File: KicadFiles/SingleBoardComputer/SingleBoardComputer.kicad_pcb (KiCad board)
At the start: 2 copper layers, 84 parts, among them J1 USB_C_Receptacle_USB2.0_16P, J2 Conn_01x06_Pin, J3 Conn_01x10_Pin, SW1 SW_DPST_x2, U1 TPS630701RNMT, U2 FT240XS, U3 LD1117S33TR_SOT223, U4 MC68000FN, U5 XC9572XL-PC44, U6 SST39SF040-70-4C-PHE, U7 SST39SF040-70-4C-PHE, U8 AS7C1026B-12JCN, Y1 CXO_DIP8

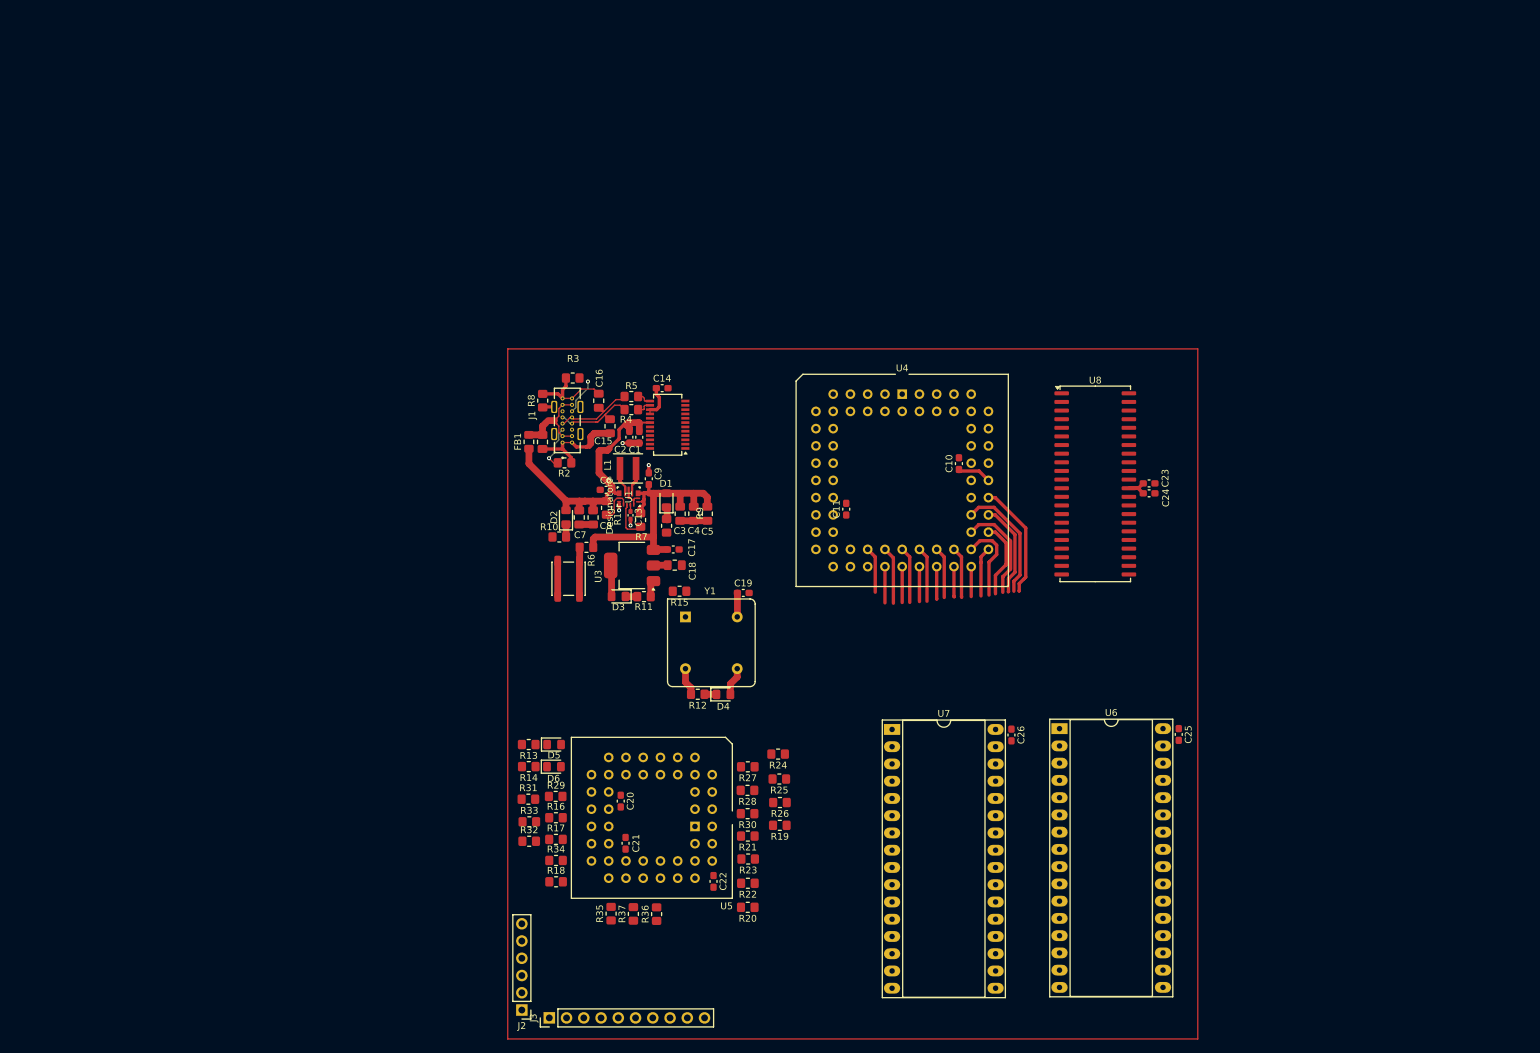
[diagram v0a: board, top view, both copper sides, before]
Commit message: PCB before schematic modification
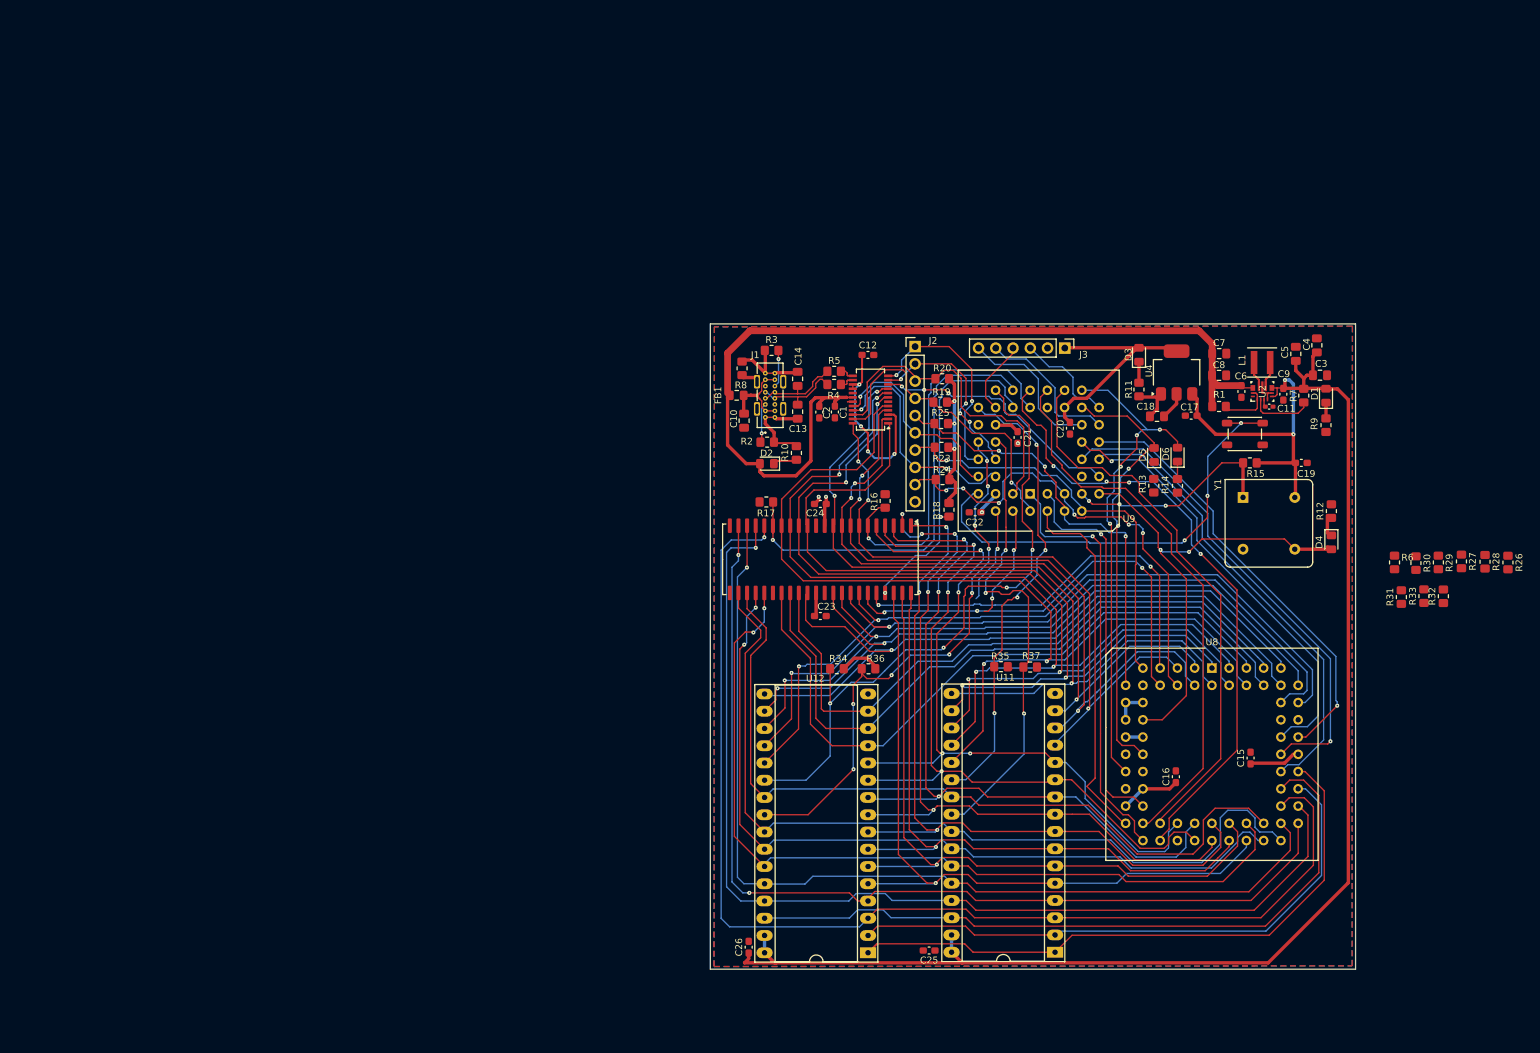
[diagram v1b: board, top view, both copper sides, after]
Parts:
- removed R21, R22: 5.1k, Resistor_SMD:R_0805_2012Metric_Pad1.20x1.40mm_HandSolder
- L1: value L -> 1.5u
- moved R32 139.3 mm to (210.8, 83.4), turned to 90 degrees
- moved R33 135.8 mm to (207.9, 83.4), turned to 90 degrees
- moved R29 134.4 mm to (210.1, 78.5), turned to -90 degrees
- moved R31 131.9 mm to (204.6, 83.5), turned to 90 degrees
- moved J3 126.1 mm to (155.1, 46.9), turned to -90 degrees
- moved R6 119.0 mm to (203.6, 78.5), turned to -90 degrees
- moved R28 113.7 mm to (216.9, 78.3), turned to -90 degrees
- moved R26 112.9 mm to (220.3, 78.5), turned to -90 degrees
- moved J2 112.6 mm to (133.0, 46.7), turned to 0 degrees
- moved R27 109.3 mm to (213.4, 78.3), turned to -90 degrees
- moved R30 105.1 mm to (206.8, 78.5), turned to -90 degrees
- moved R14 104.1 mm to (171.6, 67.2), turned to -90 degrees
- moved D6 102.7 mm to (171.7, 62.6), turned to 90 degrees
- moved SW1 101.8 mm to (181.6, 59.5), turned to 0 degrees
- moved R13 99.6 mm to (168.2, 67.2), turned to -90 degrees
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- renumbered C12 to C10, C13 to C11, C14 to C12, C15 to C13, C16 to C14, C10 to C15, C11 to C16, J3 to J2, J2 to J3, U8 to U10, U6 to U11, U7 to U12, U1 to U2, U2 to U3, U3 to U4, U4 to U8, U5 to U9
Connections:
- U9 pad 40: RegBAT -> unconnected-(U9-I/O/GTS2-Pad40)
- U9 pad 42: RegPG -> unconnected-(U9-I/O/GTS1-Pad42)
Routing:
- net +5V: track 55.3 -> 303.5 mm, vias 0 -> 6
- net A16: track 15.3 -> 170.0 mm, vias 0 -> 1
- net D7: track 0.00 -> 147.3 mm, vias 0 -> 2
- net A15: track 11.4 -> 156.4 mm, vias 0 -> 1
- net D6: track 0.00 -> 139.6 mm, vias 0 -> 4
- net A13: track 7.31 -> 146.3 mm, vias 0 -> 2
- net D5: track 0.00 -> 137.7 mm, vias 0 -> 4
- net A14: track 12.4 -> 142.7 mm, vias 0 -> 1
- net D4: track 0.00 -> 128.1 mm, vias 0 -> 2
- net D3: track 0.00 -> 125.7 mm, vias 0 -> 3
- net A12: track 4.40 -> 125.8 mm
- net A9: track 7.54 -> 125.6 mm, vias 0 -> 2
- net D14: track 0.00 -> 115.6 mm, vias 0 -> 2
- net D15: track 0.00 -> 115.1 mm, vias 0 -> 2
- net A10: track 4.47 -> 119.1 mm, vias 0 -> 2
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- added copper zone on B.Cu, net GND
- added copper zone on F.Cu, net GND
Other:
- board outline added: 95 x 95 mm

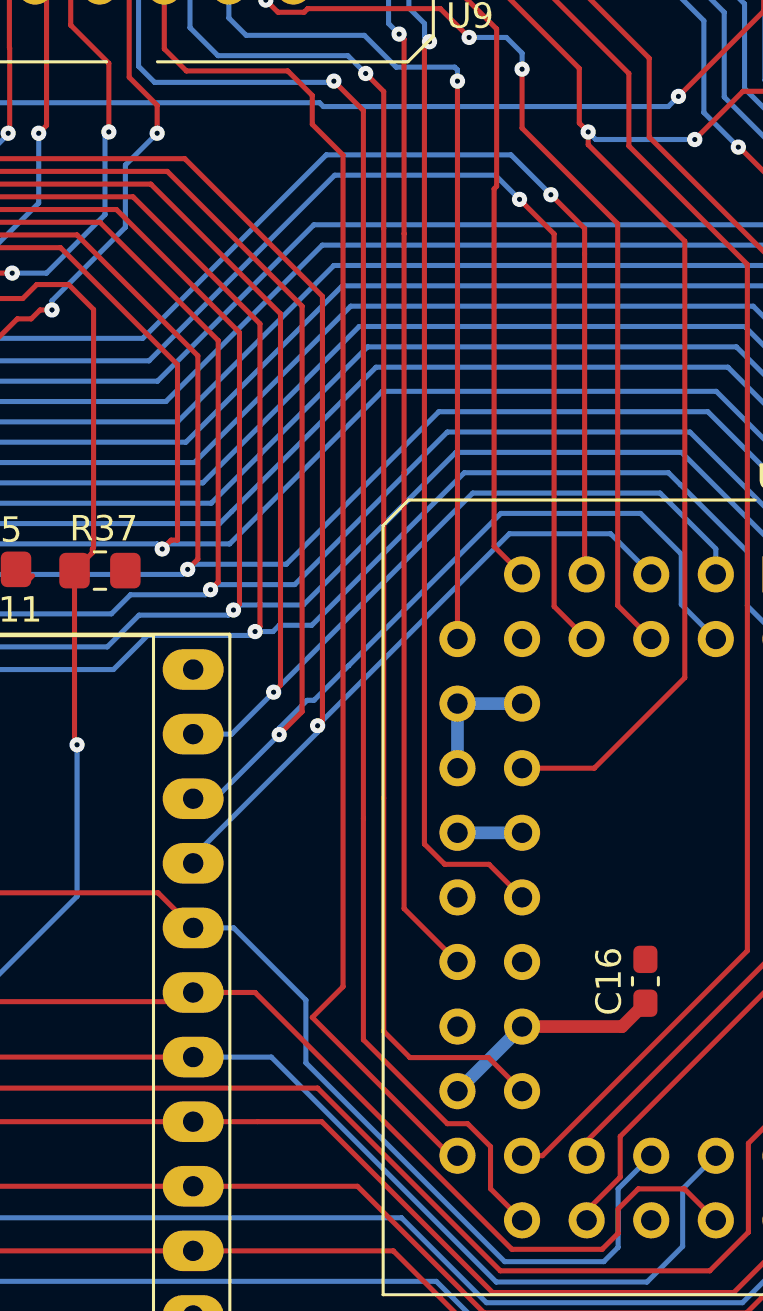
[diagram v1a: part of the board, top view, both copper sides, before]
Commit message: Schematic after corrections
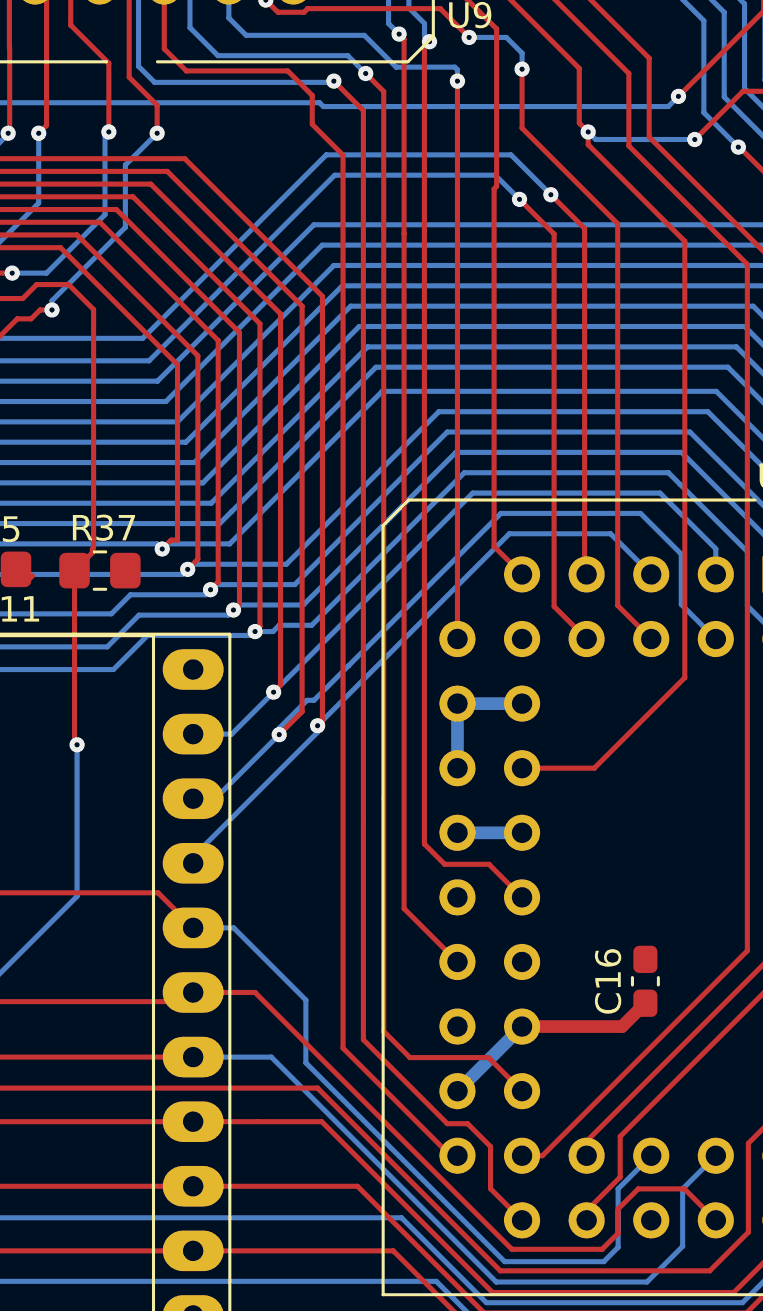
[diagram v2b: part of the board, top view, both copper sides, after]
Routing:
- net CPU_IPL1: track 54.3 -> 53.2 mm
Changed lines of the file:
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@@
 		(tags "resistor handsolder")
 		(property "Reference" "R25"
-			(at 0.1 1.6 360)
+			(at 0.1 1.6 0)
 			(layer "F.SilkS")
 			(effects
@@
 		)
 		(property "Value" "5.1k"
-			(at 0 1.65 360)
+			(at 0 1.65 0)
 			(layer "F.Fab")
 			(hide yes)
@@
 		)
 		(fp_text user "${REFERENCE}"
-			(at 0 0 360)
+			(at 0 0 0)
 			(layer "F.Fab")
 			(effects
@@
 		(tags "resistor handsolder")
 		(property "Reference" "R19"
-			(at -0.2 1.5 360)
+			(at -0.2 1.5 0)
 			(layer "F.SilkS")
 			(effects
@@
 		)
 		(property "Value" "5.1k"
-			(at 0 1.65 360)
+			(at 0 1.65 0)
 			(layer "F.Fab")
 			(hide yes)
@@
 		)
 		(fp_text user "${REFERENCE}"
-			(at 0 0 360)
+			(at 0 0 0)
 			(layer "F.Fab")
 			(effects
@@
 		(tags "resistor handsolder")
 		(property "Reference" "R17"
-			(at -0.05 1.65 360)
+			(at -0.05 1.65 0)
 			(layer "F.SilkS")
 			(effects
@@
 		)
 		(property "Value" "5.1k"
-			(at 0 1.65 360)
+			(at 0 1.65 0)
 			(layer "F.Fab")
 			(hide yes)
@@
 		)
 		(fp_text user "${REFERENCE}"
-			(at 0 0 360)
+			(at 0 0 0)
 			(layer "F.Fab")
 			(effects
@@
 		(tags "resistor handsolder")
 		(property "Reference" "R20"
-			(at 0 1.55 360)
+			(at 0 1.55 0)
 			(layer "F.SilkS")
 			(effects
@@
 		)
 		(property "Value" "5.1k"
-			(at 0 1.65 360)
+			(at 0 1.65 0)
 			(layer "F.Fab")
 			(hide yes)
@@
 		)
 		(fp_text user "${REFERENCE}"
-			(at 0 0 360)
+			(at 0 0 0)
 			(layer "F.Fab")
 			(effects
@@
 		(tags "resistor handsolder")
 		(property "Reference" "R34"
-			(at -0.2 1.5 360)
+			(at -0.2 1.5 0)
 			(layer "F.SilkS")
 			(effects
@@
 		)
 		(property "Value" "5.1k"
-			(at 0 1.65 360)
+			(at 0 1.65 0)
 			(layer "F.Fab")
 			(hide yes)
@@
 		)
 		(fp_text user "${REFERENCE}"
-			(at 0 0 360)
+			(at 0 0 0)
 			(layer "F.Fab")
 			(effects
@@
 		(tags "resistor handsolder")
 		(property "Reference" "R36"
-			(at -1.05 1.5 360)
+			(at -1.05 1.5 0)
 			(layer "F.SilkS")
 			(effects
@@
 		)
 		(property "Value" "5.1k"
-			(at 0 1.65 360)
+			(at 0 1.65 0)
 			(layer "F.Fab")
 			(hide yes)
@@
 		)
 		(fp_text user "${REFERENCE}"
-			(at 0 0 360)
+			(at 0 0 0)
 			(layer "F.Fab")
 			(effects
@@
 		(tags "resistor handsolder")
 		(property "Reference" "R24"
-			(at 0.05 1.45 360)
+			(at 0.05 1.45 0)
 			(layer "F.SilkS")
 			(effects
@@
 		)
 		(property "Value" "5.1k"
-			(at 0 1.65 360)
+			(at 0 1.65 0)
 			(layer "F.Fab")
 			(hide yes)
@@
 		)
 		(fp_text user "${REFERENCE}"
-			(at 0 0 360)
+			(at 0 0 0)
 			(layer "F.Fab")
 			(effects
@@
 		(tags "resistor handsolder")
 		(property "Reference" "R23"
-			(at 0 -1.65 360)
+			(at 0 -1.65 0)
 			(layer "F.SilkS")
 			(effects
@@
 		)
 		(property "Value" "5.1k"
-			(at 0 1.65 360)
+			(at 0 1.65 0)
 			(layer "F.Fab")
 			(hide yes)
@@
 		)
 		(fp_text user "${REFERENCE}"
-			(at 0 0 360)
+			(at 0 0 0)
 			(layer "F.Fab")
 			(effects
@@
 		(tags "resistor handsolder")
 		(property "Reference" "R37"
-			(at -0.15 1.65 360)
+			(at -0.15 1.65 0)
 			(layer "F.SilkS")
 			(effects
@@
 		)
 		(property "Value" "5.1k"
-			(at 0 1.65 360)
+			(at 0 1.65 0)
 			(layer "F.Fab")
 			(hide yes)
@@
 		)
 		(fp_text user "${REFERENCE}"
-			(at 0 0 360)
+			(at 0 0 0)
 			(layer "F.Fab")
 			(effects
@@
 	)
 	(segment
-		(start 164.01 116.86)
-		(end 163.738629 116.86)
-		(width 0.2)
-		(layer "F.Cu")
-		(net 44)
-	)
-	(segment
 		(start 153.35 74.2)
 		(end 152.4802 73.3302)
@@
 	)
 	(segment
-		(start 163.738629 116.86)
-		(end 158.3 111.421371)
+		(start 157.335786 74.2)
+		(end 153.35 74.2)
 		(width 0.2)
 		(layer "F.Cu")
@@
 	)
 	(segment
-		(start 159.51 110.211371)
-		(end 159.51 77.51)
+		(start 152.4802 73.3302)
+		(end 152.4802 70.8802)
 		(width 0.2)
 		(layer "F.Cu")
@@
 	)
 	(segment
-		(start 157.335786 74.2)
-		(end 153.35 74.2)
+		(start 163.738629 116.86)
+		(end 159.51 112.631371)
 		(width 0.2)
 		(layer "F.Cu")
@@
 	)
 	(segment
-		(start 158.3 75.164214)
-		(end 157.335786 74.2)
+		(start 164.01 116.86)
+		(end 163.738629 116.86)
 		(width 0.2)
 		(layer "F.Cu")
@@
 	)
 	(segment
-		(start 158.3 76.3)
-		(end 158.3 75.164214)
+		(start 158.3 75.164214)
+		(end 157.335786 74.2)
 		(width 0.2)
 		(layer "F.Cu")
@@
 	)
 	(segment
-		(start 152.4802 73.3302)
-		(end 152.4802 70.8802)
+		(start 159.51 77.51)
+		(end 158.3 76.3)
 		(width 0.2)
 		(layer "F.Cu")
@@
 	)
 	(segment
-		(start 158.3 111.421371)
-		(end 159.51 110.211371)
+		(start 158.3 76.3)
+		(end 158.3 75.164214)
 		(width 0.2)
 		(layer "F.Cu")
@@
 	)
 	(segment
-		(start 159.51 77.51)
-		(end 158.3 76.3)
+		(start 159.51 112.631371)
+		(end 159.51 77.51)
 		(width 0.2)
 		(layer "F.Cu")
@@
 		(min_thickness 0.25)
 		(filled_areas_thickness no)
-		(fill
+		(fill yes
 			(thermal_gap 0.5)
 			(thermal_bridge_width 0.3)

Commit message: Correction Corrections
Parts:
- added D2: LED, LED_SMD:LED_0805_2012Metric_Pad1.15x1.40mm_HandSolder, F.Cu at (78.2, 79.3)
- added D3: LED, LED_SMD:LED_0805_2012Metric_Pad1.15x1.40mm_HandSolder, F.Cu at (78.2, 82.4)
- added D4: LED, LED_SMD:LED_0805_2012Metric_Pad1.15x1.40mm_HandSolder, F.Cu at (78.2, 85.4)
- added D5: LED, LED_SMD:LED_0805_2012Metric_Pad1.15x1.40mm_HandSolder, F.Cu at (78.2, 88.5)
- added D6: LED, LED_SMD:LED_0805_2012Metric_Pad1.15x1.40mm_HandSolder, F.Cu at (78.2, 91.5)
- added J4: Conn_01x06_Pin, Connector_PinHeader_2.54mm:PinHeader_1x06_P2.54mm_Vertical, F.Cu at (51.9, 89.8)
- added J5: Conn_01x06_Pin, Connector_PinHeader_2.54mm:PinHeader_1x06_P2.54mm_Vertical, F.Cu at (56.5, 89.8)
- added R10: 1k, Resistor_SMD:R_0805_2012Metric_Pad1.20x1.40mm_HandSolder, F.Cu at (73.4, 79.3)
- added R11: 1k, Resistor_SMD:R_0805_2012Metric_Pad1.20x1.40mm_HandSolder, F.Cu at (73.4, 82.2)
- added R12: 1k, Resistor_SMD:R_0805_2012Metric_Pad1.20x1.40mm_HandSolder, F.Cu at (73.4, 85.2)
- added R13: 1k, Resistor_SMD:R_0805_2012Metric_Pad1.20x1.40mm_HandSolder, F.Cu at (73.4, 88.1)
- added R14: 1k, Resistor_SMD:R_0805_2012Metric_Pad1.20x1.40mm_HandSolder, F.Cu at (73.4, 91.1)
- added R20: 5.1k, Resistor_SMD:R_0805_2012Metric_Pad1.20x1.40mm_HandSolder, F.Cu at (73.4, 94.0)
- added SW1: SW_DPST_x2_Custom, Button_Switch_SMD:SW_SPST_PTS647_Sx38, F.Cu at (3.67, 2.73)
- added U2: TLV809EA46DBZR, Package_TO_SOT_SMD:SOT-23, F.Cu at (83.0, 80.2)
- FB1: value FerriteBead -> MI0805K601R-10
- renumbered C23 to C20, C24 to C21, C20 to C22, C21 to C23, C22 to C24, R29 to R15, R30 to R16, R31 to R17, R32 to R18, R33 to R19, R25 to R21, R19 to R22, R20 to R23, R26 to R24, R27 to R25, R28 to R26, R16 to R27, R17 to R28, R18 to R29, U9 to U11, U11 to U12, U12 to U13, U2 to U3, U3 to U4, U4 to U5, U8 to U9
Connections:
- D1 pad 1: Net-(D1-K) -> GND
- D1 pad 2: +5V -> Net-(D1-A)
- R15 pad 2: CPU_RST -> CPU_IPL2
- R16 pad 2: CPU_HALT -> CPU_IPL1
- R17 pad 2: CPU_FC0 -> CPU_IPL0
- R18 pad 2: CPU_FC1 -> CPU_HALT
- R19 pad 2: CPU_FC2 -> CPU_RST
- R21 pad 2: CPU_DTACK -> ROM_0_CE
- R22 pad 2: UTP_CBUS5 -> ROM_1_CE
- R23 pad 2: UTP_CBUS6 -> ROM_0_OE
- R24 pad 2: CPU_IPL2 -> ROM_1_OE
- R25 pad 2: CPU_IPL1 -> D0
- R26 pad 2: CPU_IPL0 -> CPU_DTACK
- R6 pad 2: R_BTN -> Net-(SW1A-A)
- R9 pad 1: Net-(D1-K) -> +5V
- R9 pad 2: GND -> Net-(D1-A)
- SW1 pad 1: R_BTN -> Net-(SW1A-A)
- U11 pad 1: CPU_IPL0 -> CPU_LDS
- U11 pad 11: A20 -> CPU_AS
- U11 pad 12: A21 -> CPU_IPL2
- U11 pad 13: A22 -> CPU_IPL1
- U11 pad 14: A23 -> CPU_IPL0
- U11 pad 18: CPU_RST -> CPU_HALT
- U11 pad 19: CPU_HALT -> CPU_RST
- U11 pad 2: CPU_IPL1 -> CPU_UDS
- U11 pad 20: CPU_FC0 -> CPU_FC2
- U11 pad 22: CPU_FC2 -> CPU_FC0
- U11 pad 25: RAM_CE -> A19
- U11 pad 26: RAM_WE -> A20
- U11 pad 27: RAM_OE -> UTP_WR
- U11 pad 28: ROM_0_CE -> UTP_RD
- U11 pad 29: ROM_1_CE -> UTP_RST
- U11 pad 3: CPU_IPL2 -> RAM_OE
- U11 pad 33: ROM_0_OE -> UTP_CBUS5
- U11 pad 34: ROM_1_OE -> UTP_CBUS6
- U11 pad 35: UTP_WR -> UTP_TXE
- U11 pad 36: UTP_RD -> UTP_RXF
- U11 pad 37: UTP_TXE -> CPU_R/W
- U11 pad 38: UTP_RXF -> UTP_SIWU
- U11 pad 39: R_BTN -> D0
- U11 pad 4: CPU_DTACK -> RAM_WE
- U11 pad 40: unconnected-(U9-I/O/GTS2-Pad40) -> ROM_1_OE
- U11 pad 42: unconnected-(U9-I/O/GTS1-Pad42) -> ROM_0_OE
- U11 pad 43: UTP_CBUS6 -> ROM_1_CE
- U11 pad 44: UTP_CBUS5 -> ROM_0_CE
- U11 pad 5: CPU_AS -> RAM_CE
- U11 pad 6: CPU_R/W -> CLK
- U11 pad 7: CLK -> R_BTN
- U11 pad 9: UTP_SIWU -> CPU_DTACK
- U12 pad 1: A19 -> GND
- U13 pad 1: A19 -> GND
- U4 pad 16: UTP_3V3 -> UTP_RST
- U9 pad 53: A21 -> unconnected-(U9-A21-Pad53)
- U9 pad 54: A22 -> unconnected-(U9-A22-Pad54)
- U9 pad 55: A23 -> unconnected-(U9-A23-Pad55)
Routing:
- net A21: track 72.2 -> 0.00 mm, vias 1 -> 0
- net CPU_IPL2: track 56.6 -> 128.8 mm, vias 1 -> 2
- net D0: track 97.5 -> 163.3 mm, vias 3 -> 6
- net R_BTN: track 65.8 -> 0.00 mm, vias 3 -> 0
- net A23: track 65.1 -> 0.00 mm, vias 1 -> 0
- net CPU_IPL0: track 62.6 -> 127.7 mm, vias 1 -> 2
- net CPU_IPL1: track 53.2 -> 118.1 mm, vias 0 -> 1
- net A22: track 64.9 -> 0.00 mm, vias 1 -> 0
- net unconnected-(U9-I/O/GTS1-Pad42): track 17.3 -> 0.00 mm, vias 2 -> 0
- net ROM_0_OE: track 82.8 -> 100.0 mm, vias 9 -> 11
- net unconnected-(U9-I/O/GTS2-Pad40): track 14.4 -> 0.00 mm, vias 1 -> 0
- net ROM_1_OE: track 69.5 -> 83.9 mm, vias 3 -> 4
- net Net-(D1-K): track 2.32 -> 0.00 mm
- net (no net): track 0.00 -> 2.32 mm
